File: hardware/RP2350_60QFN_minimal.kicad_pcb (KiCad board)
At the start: 4 copper layers, 106.9 x 43.5 mm, 137 parts, among them J1 UJ20-C-H-G-SMT-2A-P16-TR, J2 73101-0570, J3 73101-0570, J4 PinHeader_1x03, J5 4677, SW1 SW_Push, SW2 SW_Push, U1 RP2350_60QFN, U10 ADG621BRMZ, U13 TLP3441TP_F, U15 ADG621BRMZ, U2 REF35330QDBVR, U3 W25Q128JVS, U4 LM27762, U5 NCP1117-3.3_SOT223, U6 MCP47FEB02A0T-E/ST, U7 Opamp_Dual, U8 TLP3441TP_F, Y1 ABM8-272-T3

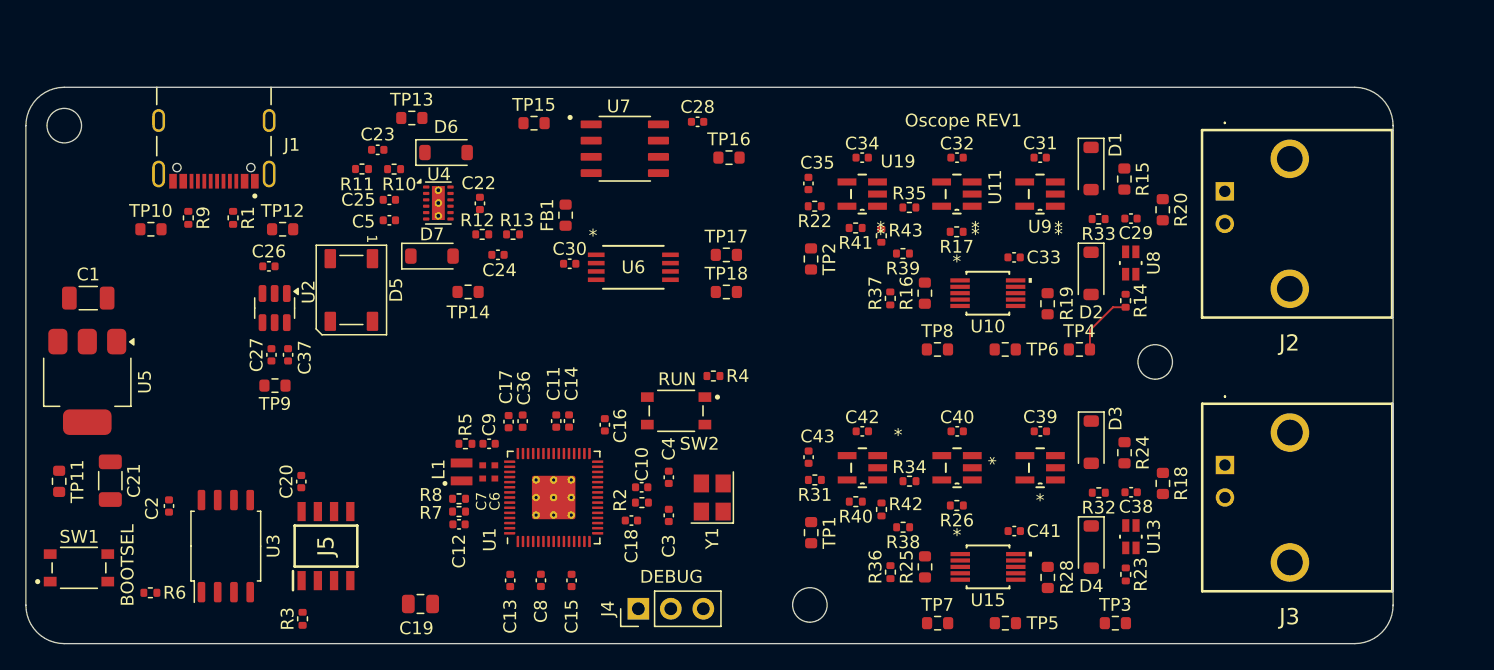
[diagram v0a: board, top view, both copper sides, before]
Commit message: feat(hardware): Route mcu
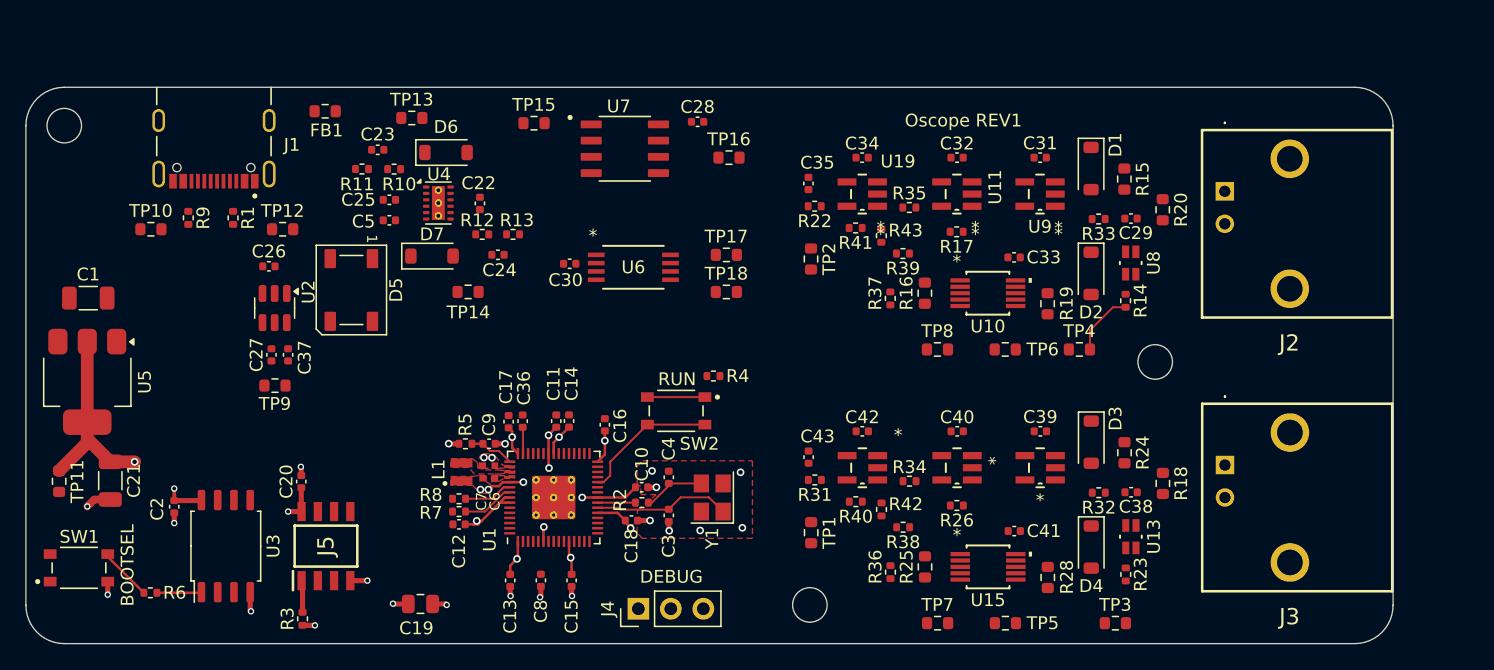
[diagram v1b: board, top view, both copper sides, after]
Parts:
- moved FB1 20.5 mm to (118.1, 97.1), turned to 0 degrees
- moved C2 0.42 mm to (106.3, 128.0)
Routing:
- net +3V3: track 0.00 -> 46.5 mm, vias 0 -> 13
- net +1V1: track 0.00 -> 15.8 mm, vias 0 -> 7
- net GND: track 0.00 -> 14.0 mm, vias 0 -> 20
- net /RUN: track 0.00 -> 10.9 mm
- net /XIN: track 0.00 -> 10.7 mm
- net Net-(C4-Pad1): track 0.00 -> 4.87 mm
- net Net-(R4-Pad1): track 0.00 -> 4.50 mm
- net /~{USB_BOOT}: track 0.00 -> 4.19 mm
- net Net-(U1-USB_DP): track 0.00 -> 4.07 mm
- net Net-(U1-USB_DM): track 0.00 -> 3.83 mm
- net /VREG_AVDD: track 0.00 -> 3.53 mm
- net /~{FLASH_CS}: track 0.00 -> 3.51 mm
- net /XOUT: track 0.00 -> 2.95 mm
- net /~{PSRAM_CS}: track 0.00 -> 2.51 mm
- net /VREF: track 0.00 -> 2.06 mm
- added copper zone on F.Cu, net +1V1
- added copper zone on In2.Cu, net +1V1
- added copper zone on F.Cu, net +3V3
- added copper zone on In2.Cu, net +3V3
- added copper zone on In2.Cu, net +3V3A
- added copper zone on F.Cu, net /VREG_LX
- added copper zone on F.Cu, net GND
- added copper zone on In1.Cu, net GND

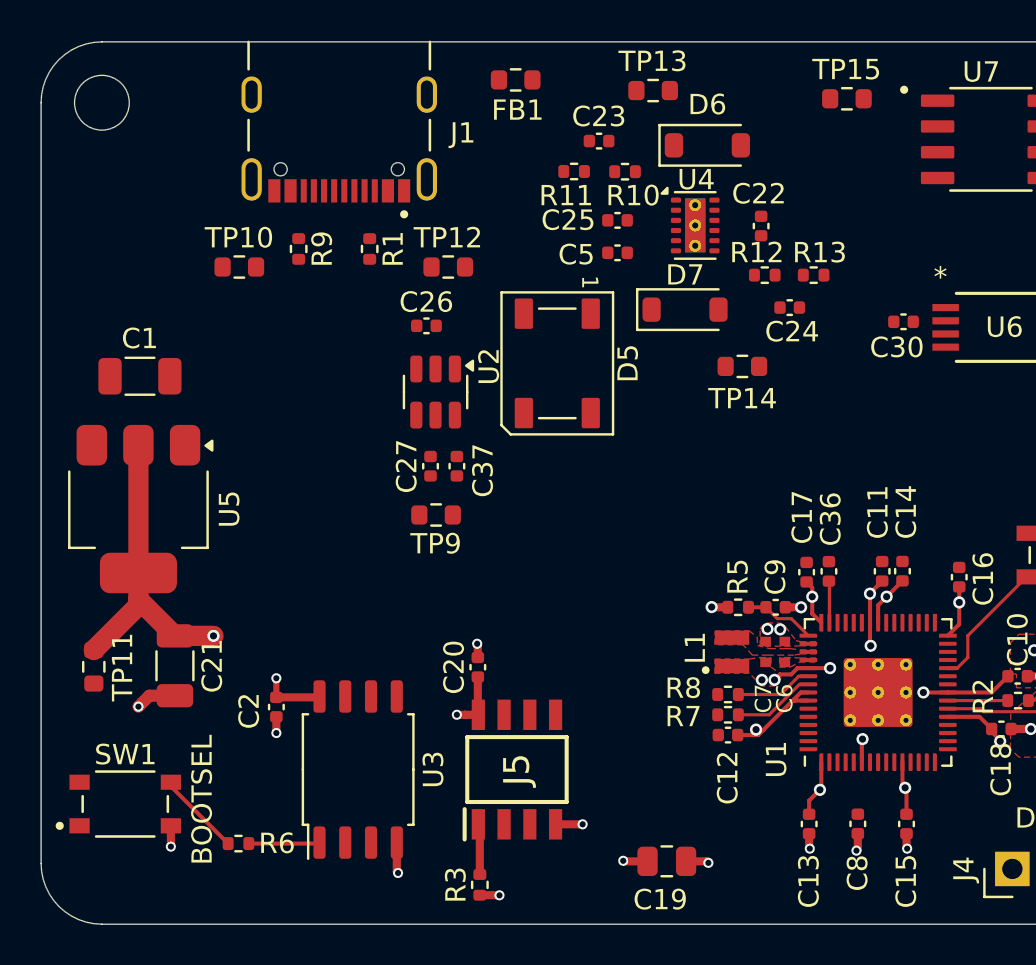
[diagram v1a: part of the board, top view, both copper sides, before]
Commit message: feat(hardware): Add VBUS plane
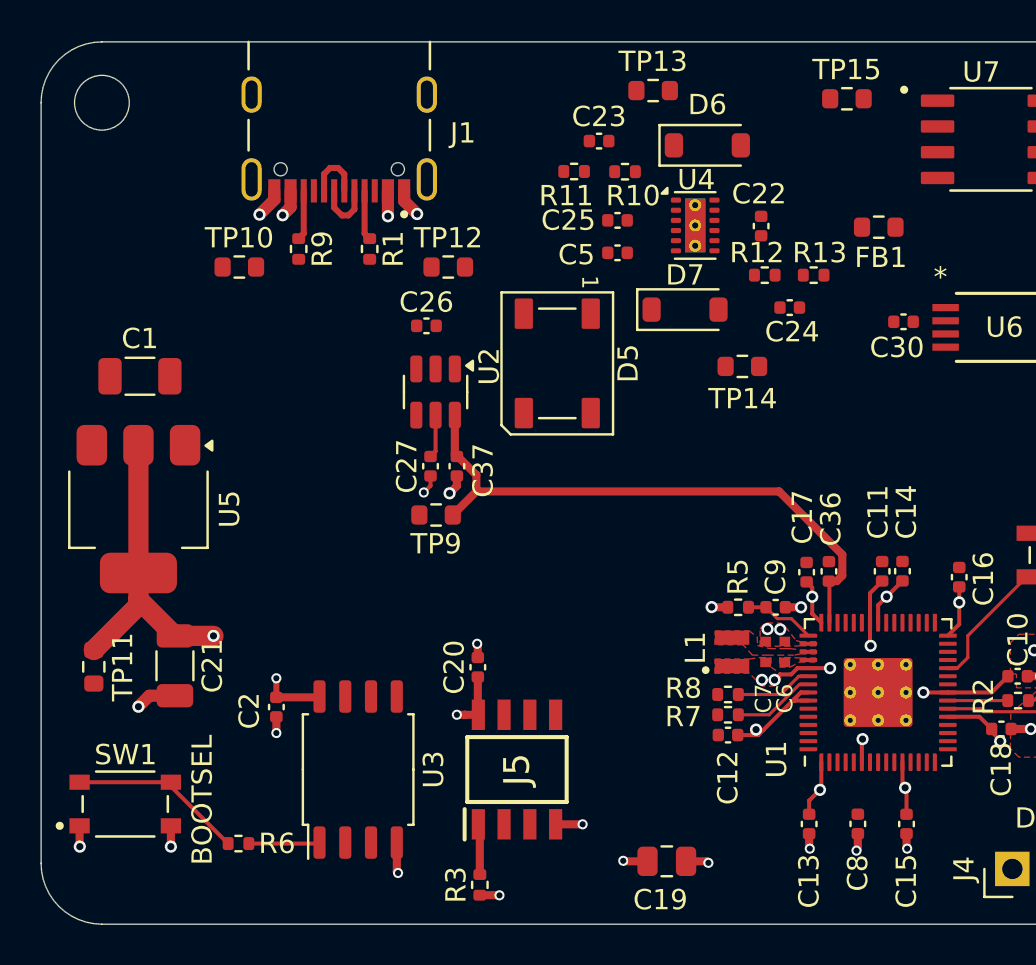
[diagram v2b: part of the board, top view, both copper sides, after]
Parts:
- moved FB1 19.3 mm to (136.0, 104.4)
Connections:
- R1 pad 1: /PSU/UCB_CC1 -> /PSU/USB_CC1
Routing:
- net /VREF: track 2.06 -> 29.1 mm
- net GND: track 14.0 -> 19.9 mm, vias 20 -> 25
- net /~{USB_BOOT}: track 4.19 -> 8.69 mm
- net /USB_D-: track 0.00 -> 3.02 mm
- net /USB_D+: track 0.00 -> 2.91 mm
- net VBUS: track 0.00 -> 2.61 mm, vias 0 -> 2
- net /PSU/USB_CC2: track 0.00 -> 2.46 mm
- net /PSU/USB_CC1: track 0.00 -> 2.46 mm
- net Net-(U2-NR): track 0.00 -> 2.14 mm
- net +1V1: vias 7 -> 6
- added copper zone on In2.Cu, net VBUS

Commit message: feat(hardware): Janky flash QSPI length matching
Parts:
- moved FB1 22.7 mm to (151.3, 121.1)
- moved R6 11.2 mm to (115.6, 135.2), turned to -90 degrees
- moved C20 9.56 mm to (106.7, 127.1)
- moved C2 9.51 mm to (115.8, 127.1), turned to 90 degrees
- moved U3 9.11 mm to (119.4, 131.1)
- moved J5 7.87 mm to (110.3, 130.3)
- moved R3 7.87 mm to (108.5, 136.0)
- moved C19 1.53 mm to (127.1, 135.6)
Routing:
- net /QSPI_SD3: track 0.00 -> 19.9 mm
- net /QSPI_SCLK: track 0.00 -> 19.6 mm
- net /QSPI_SD1: track 0.00 -> 19.4 mm
- net /QSPI_SD0: track 0.00 -> 19.2 mm
- net /QSPI_SD2: track 0.00 -> 19.1 mm
- net /~{USB_BOOT}: track 8.69 -> 25.2 mm, vias 0 -> 2
- net /~{FLASH_CS}: track 3.51 -> 19.0 mm
- net GND: track 19.9 -> 34.9 mm, vias 25 -> 34
- net VBUS: track 2.61 -> 14.3 mm, vias 2 -> 7
- net +3V3: track 46.5 -> 45.8 mm

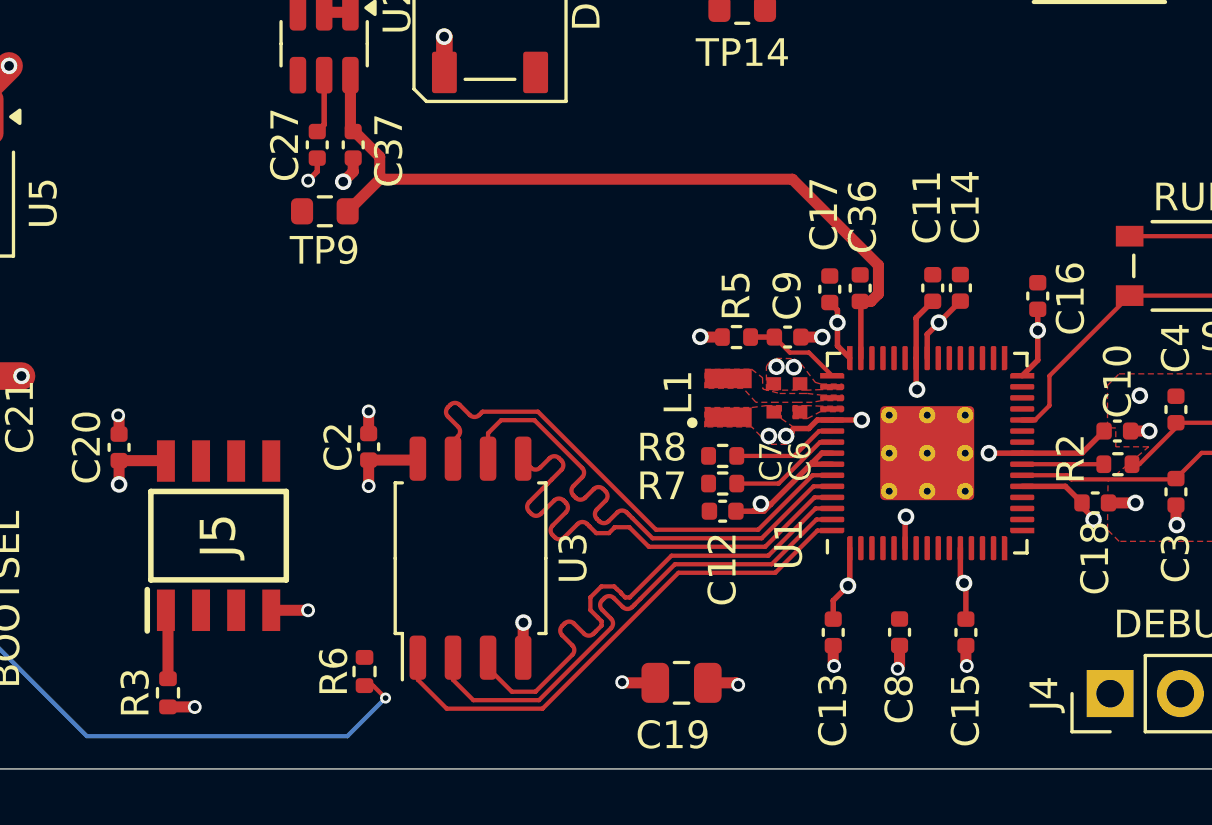
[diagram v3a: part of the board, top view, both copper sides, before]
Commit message: feat(hardware): PSRAM length matching
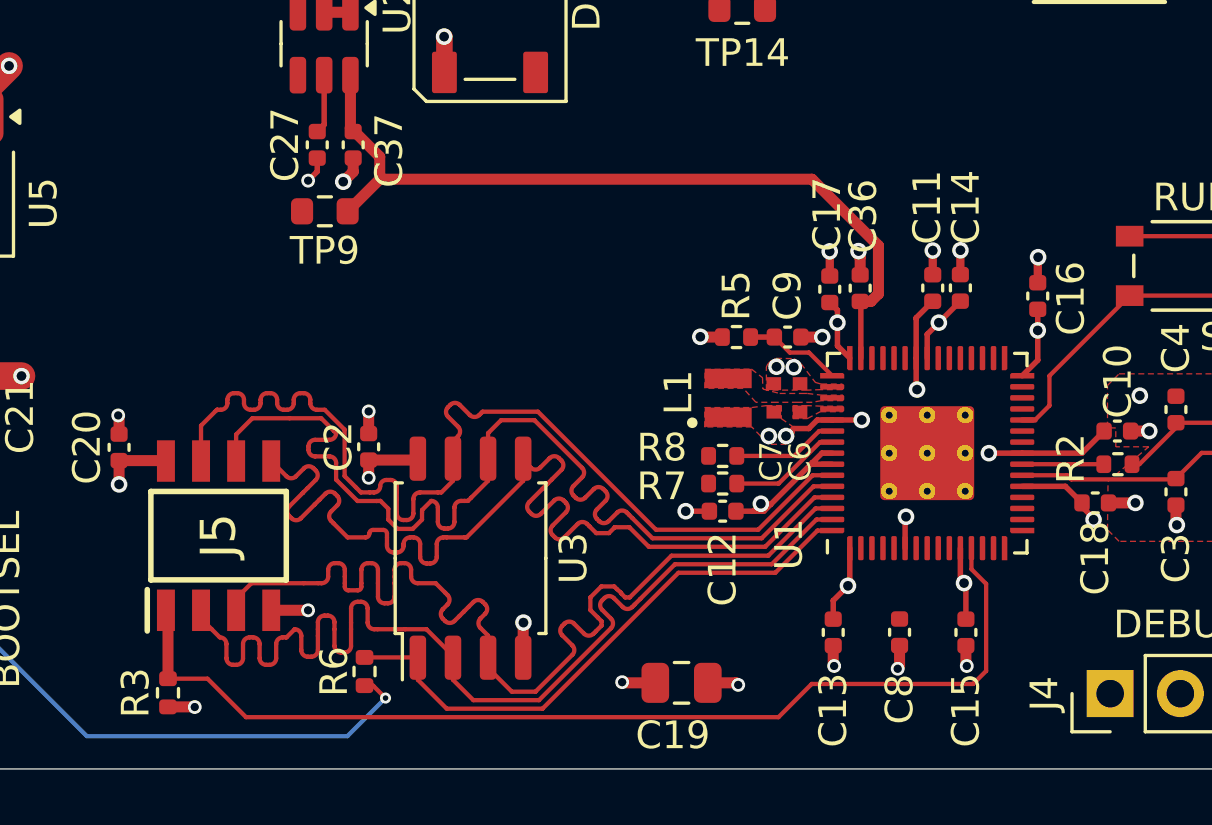
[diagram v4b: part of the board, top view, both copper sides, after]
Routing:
- net /~{PSRAM_CS}: track 2.51 -> 38.0 mm
- net /QSPI_SD2: track 19.1 -> 37.8 mm
- net /QSPI_SD0: track 19.2 -> 37.7 mm
- net /QSPI_SD1: track 19.4 -> 37.8 mm
- net /QSPI_SD3: track 19.9 -> 37.8 mm
- net /QSPI_SCLK: track 19.6 -> 37.4 mm
- net GND: track 34.9 -> 40.2 mm, vias 34 -> 40
- net /~{FLASH_CS}: track 19.0 -> 20.9 mm

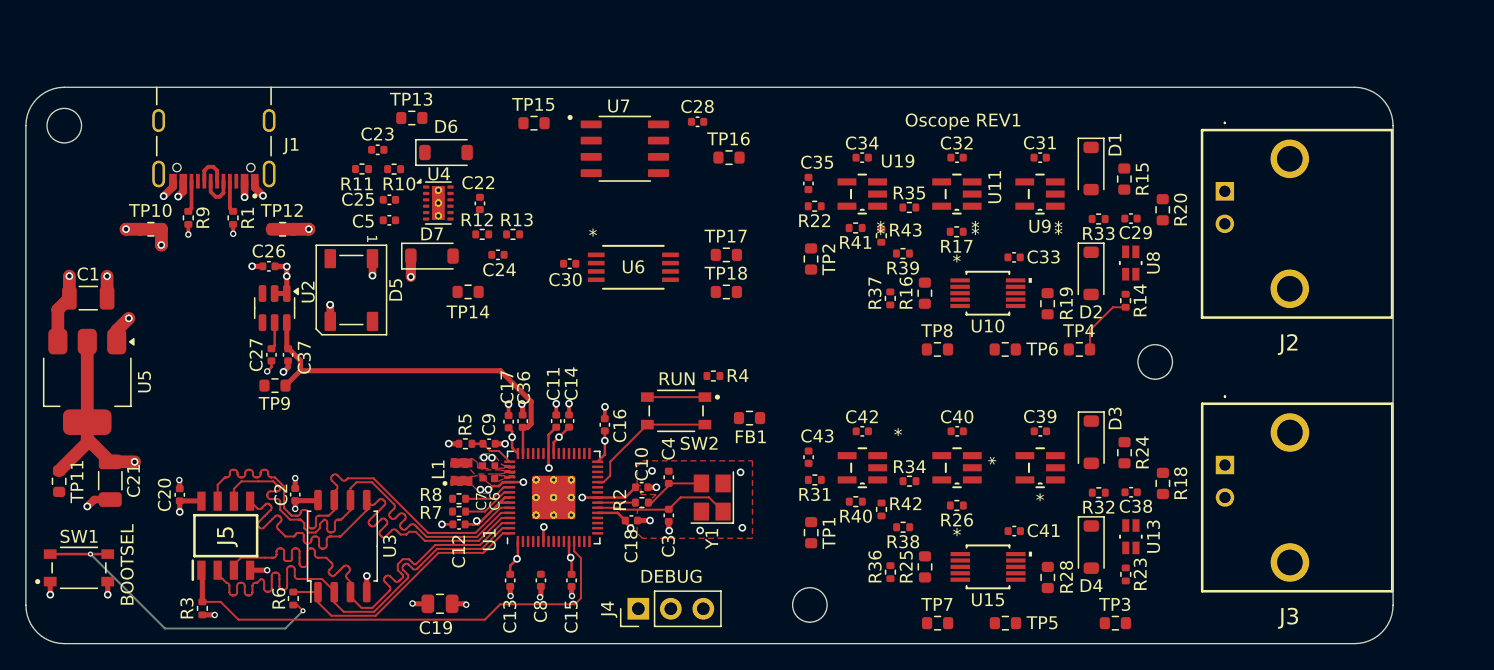
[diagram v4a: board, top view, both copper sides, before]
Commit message: feat(hardware): Add 1v65 rail on 4th plane
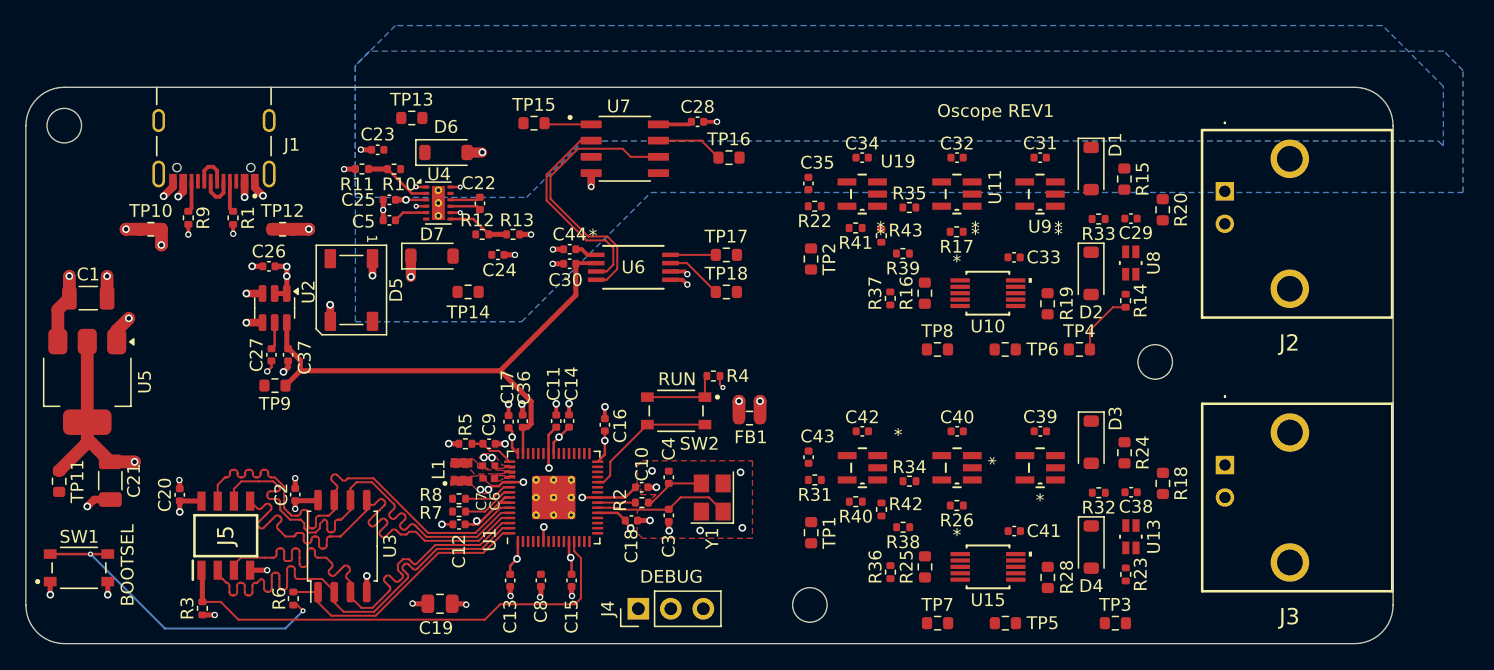
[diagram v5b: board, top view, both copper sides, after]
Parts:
- added C44: 100n, Capacitor_SMD:C_0402_1005Metric, F.Cu at (137.2, 107.9)
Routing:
- net /Trigger/CHB_COMP: track 0.00 -> 21.9 mm
- net /Trigger/CHA_COMP: track 0.00 -> 16.2 mm
- net GND: track 40.2 -> 55.8 mm, vias 40 -> 55
- net /VREF: track 29.5 -> 41.9 mm
- net VBUS: track 14.3 -> 20.7 mm, vias 7 -> 12
- net /PSU/FB+: track 0.00 -> 5.30 mm
- net /CHB_TRIG: track 0.00 -> 5.24 mm
- net /PSU/FB-: track 0.00 -> 4.88 mm
- net /TRIG_SDA: track 0.00 -> 4.48 mm
- net +3V3A: track 0.00 -> 3.98 mm, vias 0 -> 1
- net /CHA_TRIG: track 0.00 -> 3.68 mm
- net /TRIG_SCL: track 0.00 -> 3.55 mm
- net +3V3: track 45.5 -> 48.6 mm, vias 13 -> 14
- net Net-(U4-CP): track 0.00 -> 2.65 mm
- net Net-(U4-C-): track 0.00 -> 2.41 mm
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- added copper zone on B.Cu, net +1V65
- added copper zone on B.Cu, net -1V65

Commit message: feat(hardware): Add fill zones for 1v65 rails, route charge pump
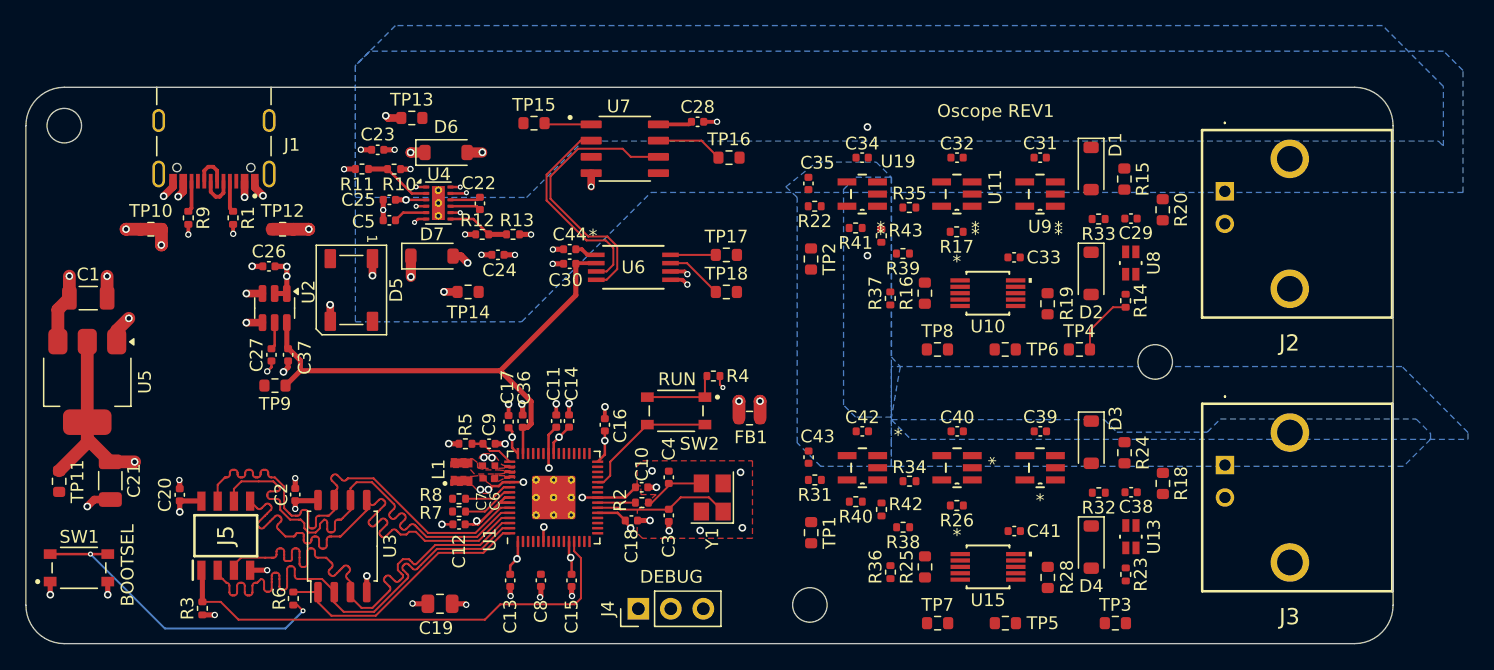
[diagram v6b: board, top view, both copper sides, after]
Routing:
- net +1V65: track 0.00 -> 15.4 mm, vias 0 -> 7
- net -1V65: track 0.00 -> 5.09 mm, vias 0 -> 5
